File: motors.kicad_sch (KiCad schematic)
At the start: 32 parts, among them Q1 NMOS, Q2 NMOS, Q3 NMOS, Q4 NMOS

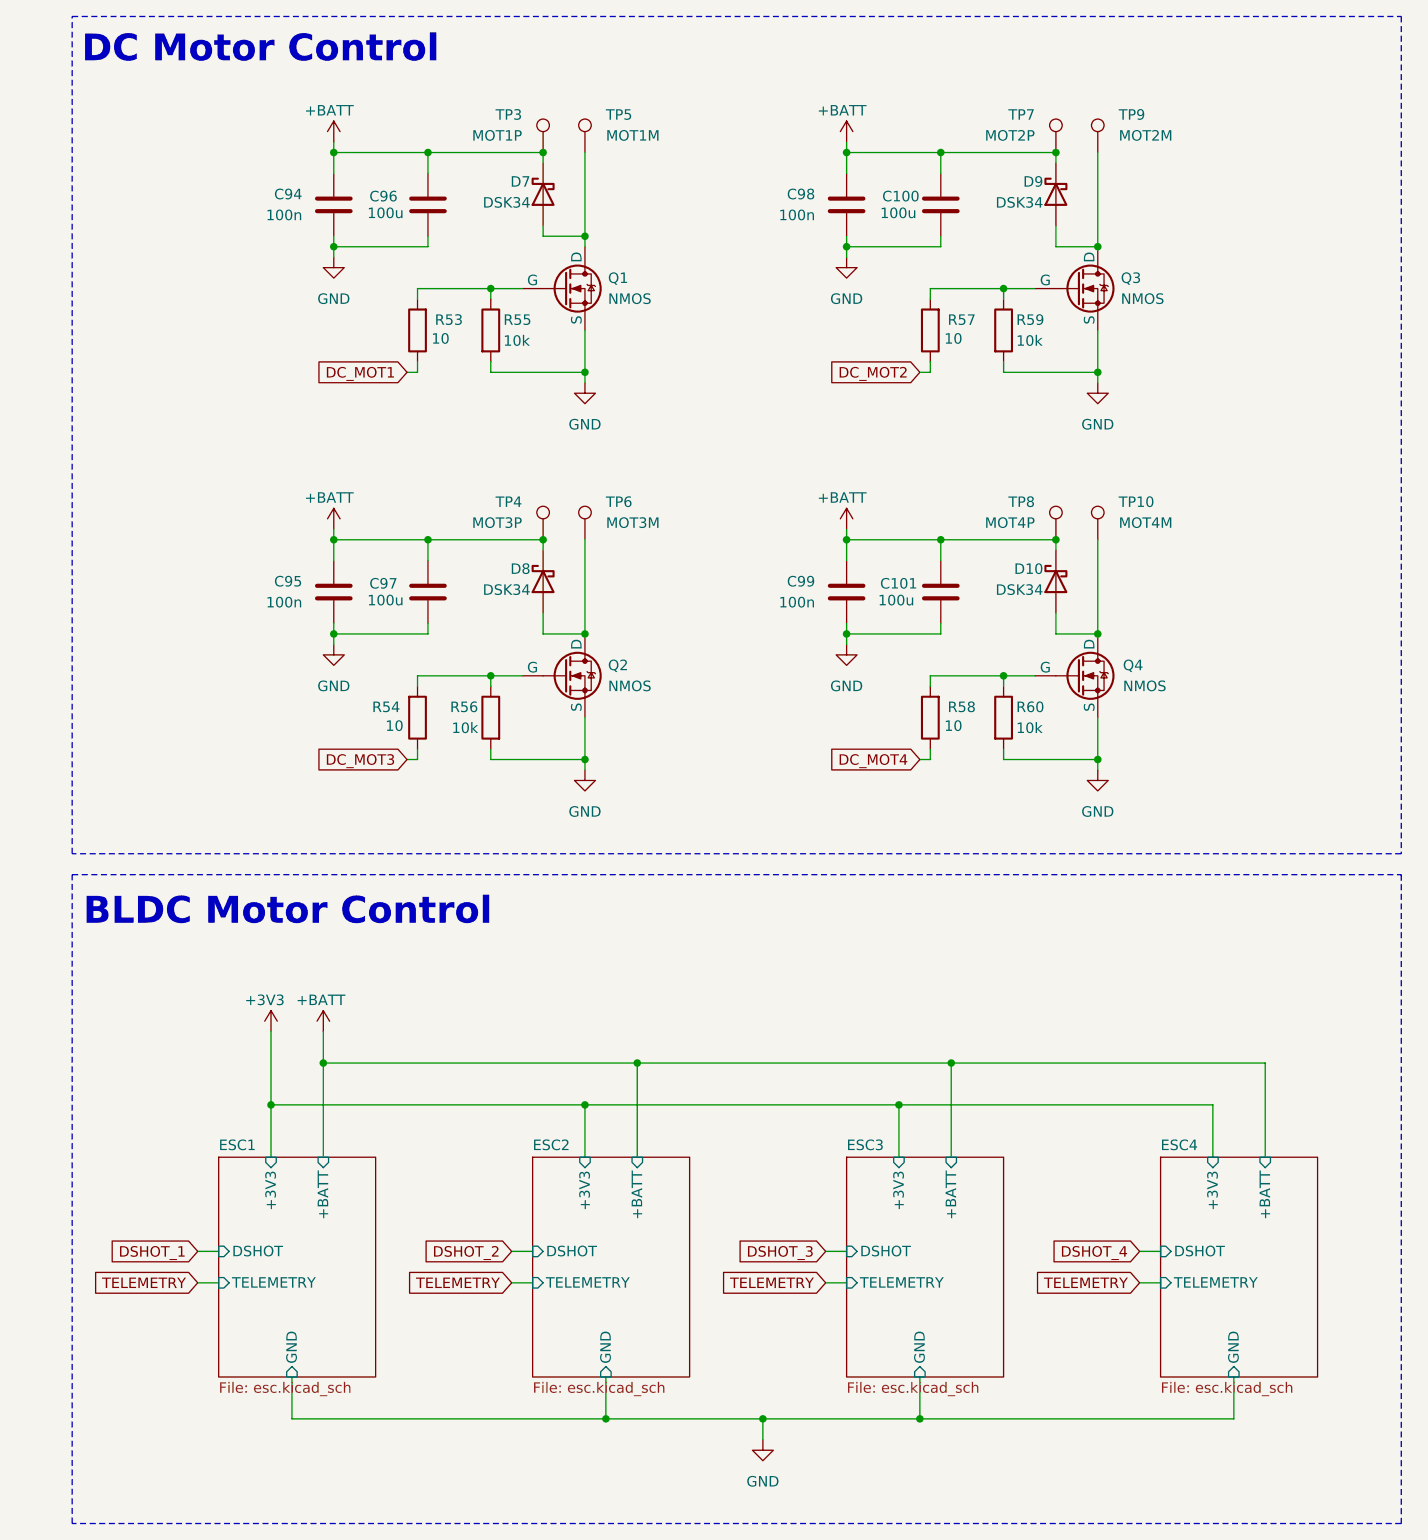
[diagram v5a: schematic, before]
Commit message: Remove brushed motor control and WS2812B LEDs
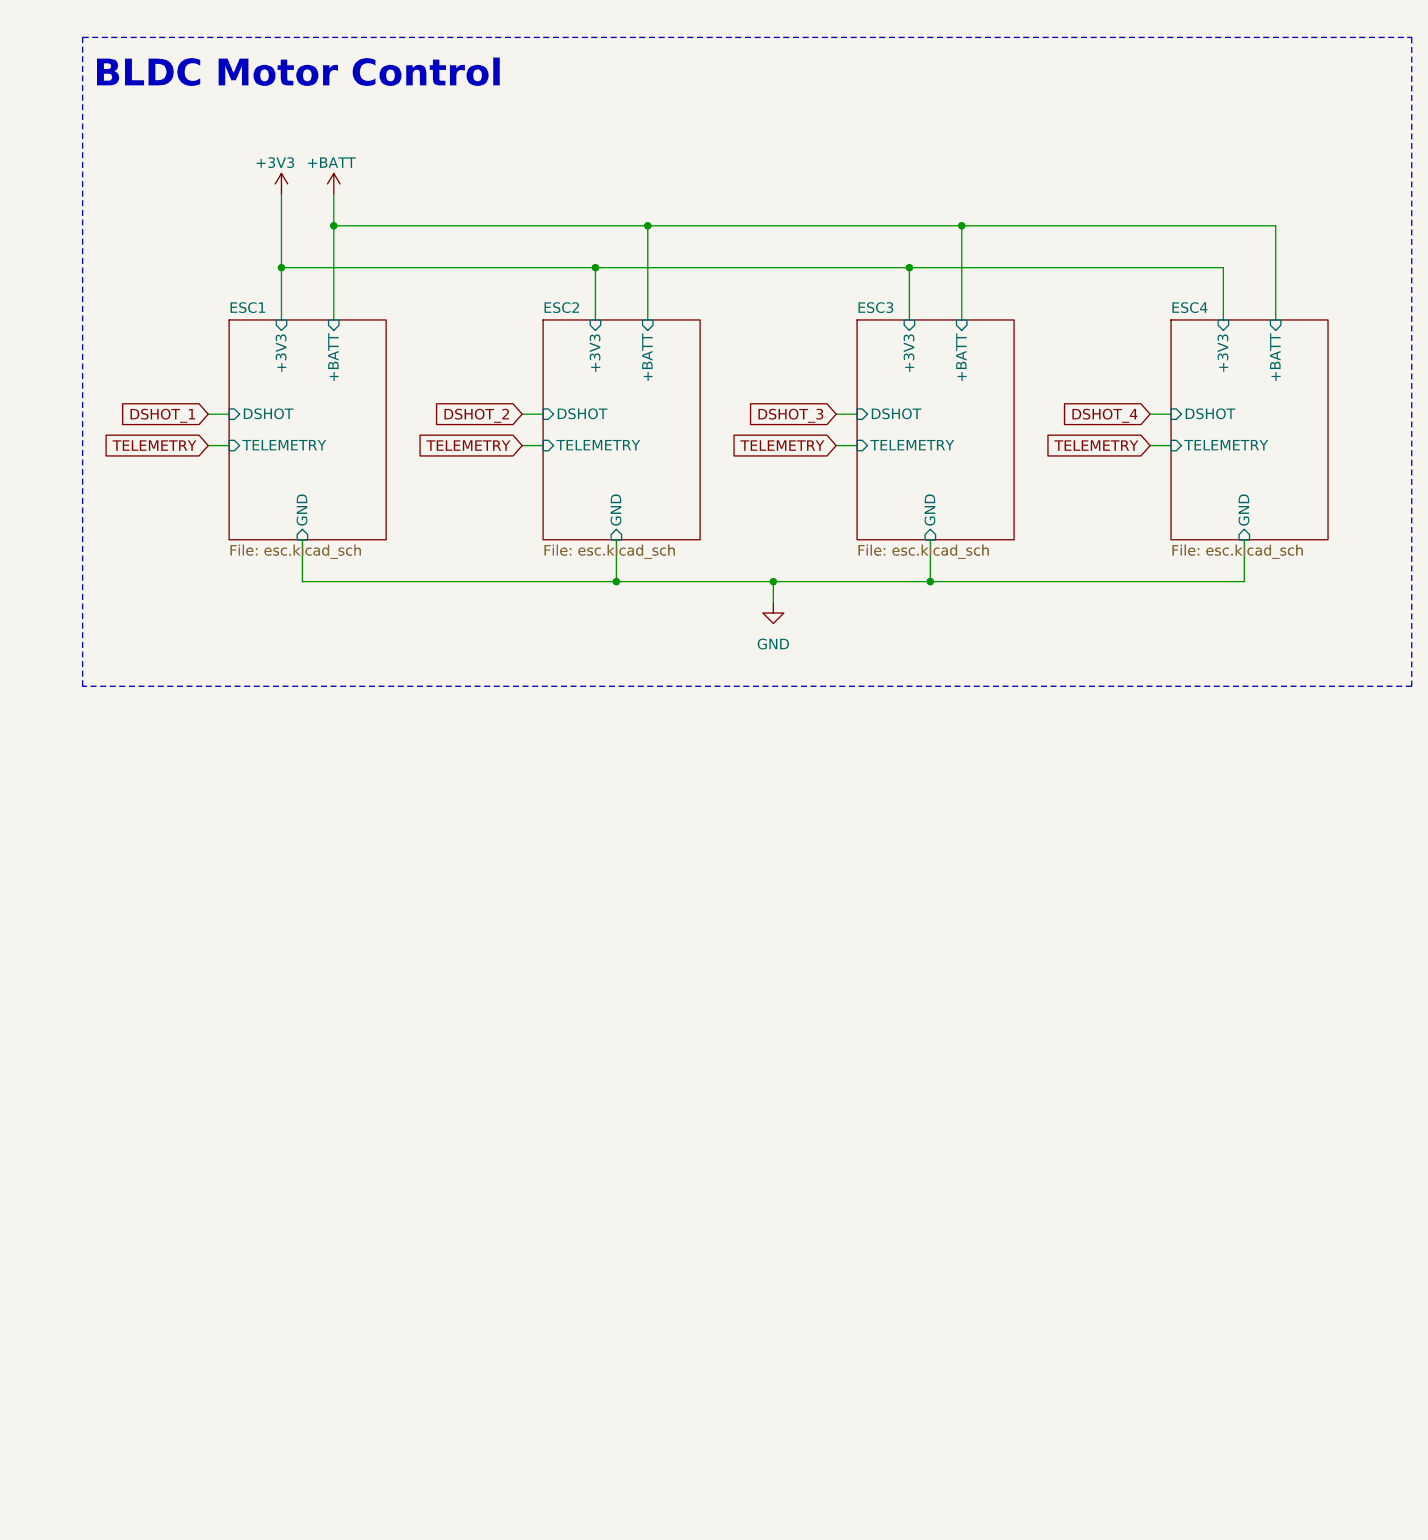
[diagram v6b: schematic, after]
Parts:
- removed C100, C101, C96, C97: 100u, Capacitor_SMD:C_1206_3216Metric, symbol Device:C
- removed C94, C95, C98, C99: 100n, Capacitor_SMD:C_0402_1005Metric, symbol Device:C
- removed D10, D7, D8, D9: DSK34, Diode_SMD:D_SOD-123F, symbol Device:D_Schottky
- removed Q1, Q2, Q3, Q4: NMOS, easyeda2kicad:SOT-23-IRLML6344, symbol Simulation_SPICE:NMOS
- removed R53, R54, R57, R58: 10, Resistor_SMD:R_0402_1005Metric, symbol Device:R
- removed R55, R56, R59, R60: 10k, Resistor_SMD:R_0402_1005Metric, symbol Device:R
- removed TP10: MOT4M, easyeda2kicad:MotorPad_1x3mm, symbol Connector:TestPoint
- removed TP3: MOT1P, easyeda2kicad:MotorPad_1x3mm, symbol Connector:TestPoint
- removed TP4: MOT3P, easyeda2kicad:MotorPad_1x3mm, symbol Connector:TestPoint
- removed TP5: MOT1M, easyeda2kicad:MotorPad_1x3mm, symbol Connector:TestPoint
- removed TP6: MOT3M, easyeda2kicad:MotorPad_1x3mm, symbol Connector:TestPoint
- removed TP7: MOT2P, easyeda2kicad:MotorPad_1x3mm, symbol Connector:TestPoint
- removed TP8: MOT4P, easyeda2kicad:MotorPad_1x3mm, symbol Connector:TestPoint
- removed TP9: MOT2M, easyeda2kicad:MotorPad_1x3mm, symbol Connector:TestPoint
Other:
- note removed: "DC Motor Control"

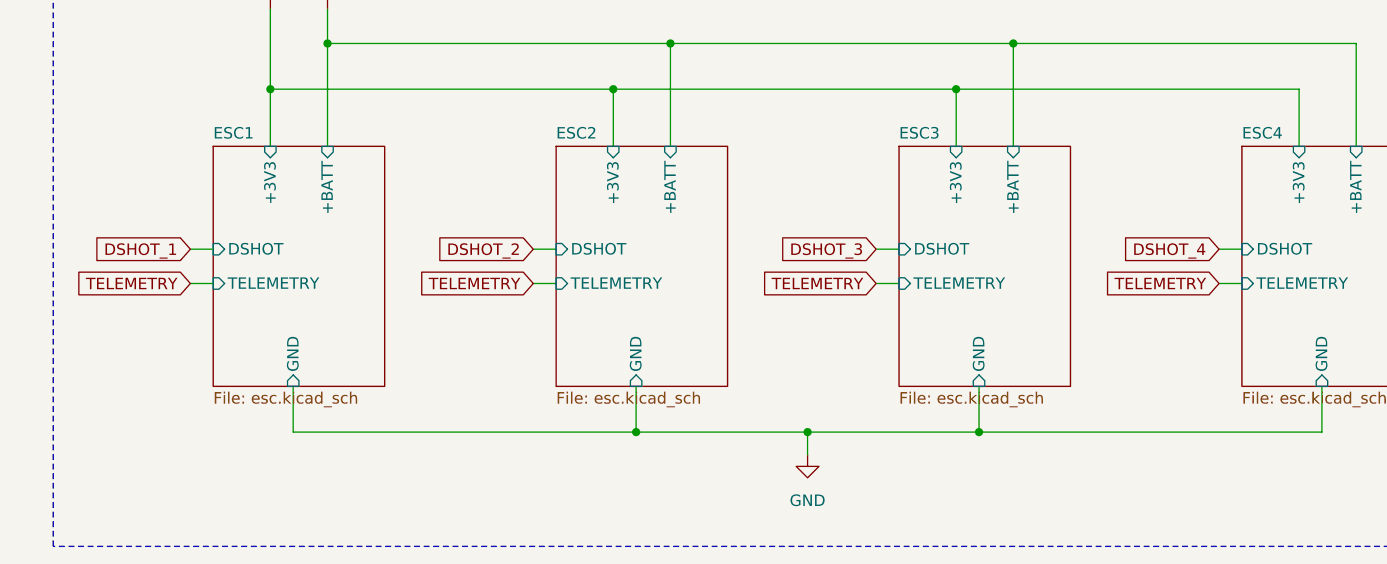
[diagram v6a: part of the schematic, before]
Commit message: Remove external SPI connections and switch voltage measurement from VBUS to +BAT
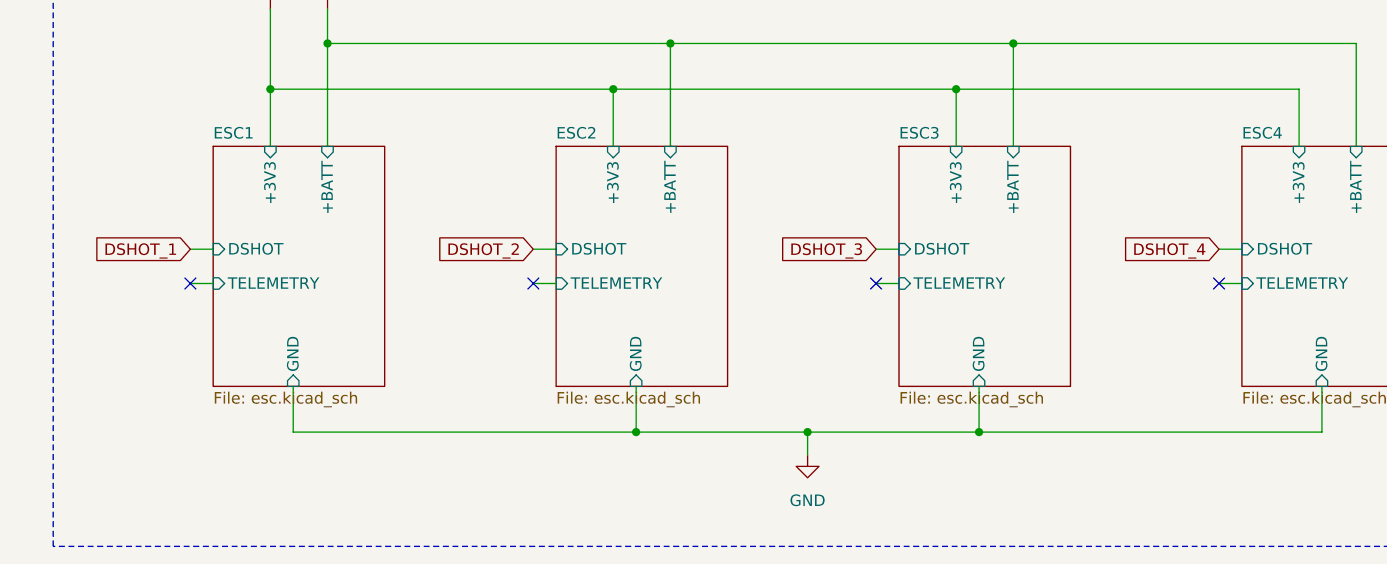
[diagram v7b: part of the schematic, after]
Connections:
- no-connect marks 0 -> 4
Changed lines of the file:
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@@
 		(color 0 0 0 0)
+	)
+	(no_connect
+		(at 144.78 66.04)
+	)
+	(no_connect
+		(at 68.58 66.04)
+	)
+	(no_connect
+		(at 106.68 66.04)
+	)
+	(no_connect
+		(at 30.48 66.04)
 	)
 	(wire
@@
 		)
 	)
-	(global_label "TELEMETRY"
-		(shape input)
-		(at 68.58 66.04 180)
-		(fields_autoplaced yes)
-		(effects
-			(font
-				(size 1.27 1.27)
-			)
-			(justify right)
-		)
-		(property "Intersheetrefs" "${INTERSHEET_REFS}"
-			(at 55.3745 66.04 0)
-			(hide yes)
-			(show_name no)
-			(do_not_autoplace no)
-			(effects
-				(font
-					(size 1.27 1.27)
-				)
-				(justify right)
-			)
-		)
-	)
 	(global_label "DSHOT_3"
 		(shape input)
@@
 		)
 	)
-	(global_label "TELEMETRY"
-		(shape input)
-		(at 144.78 66.04 180)
-		(fields_autoplaced yes)
-		(effects
-			(font
-				(size 1.27 1.27)
-			)
-			(justify right)
-		)
-		(property "Intersheetrefs" "${INTERSHEET_REFS}"
-			(at 131.5745 66.04 0)
-			(hide yes)
-			(show_name no)
-			(do_not_autoplace no)
-			(effects
-				(font
-					(size 1.27 1.27)
-				)
-				(justify right)
-			)
-		)
-	)
 	(global_label "DSHOT_4"
 		(shape input)
@@
 			(hide yes)
 			(show_name no)
-			(do_not_autoplace no)
-			(effects
-				(font
-					(size 1.27 1.27)
-				)
-				(justify right)
-			)
-		)
-	)
-	(global_label "TELEMETRY"
-		(shape input)
-		(at 106.68 66.04 180)
-		(fields_autoplaced yes)
-		(effects
-			(font
-				(size 1.27 1.27)
-			)
-			(justify right)
-		)
-		(property "Intersheetrefs" "${INTERSHEET_REFS}"
-			(at 93.4745 66.04 0)
-			(hide yes)
-			(show_name no)
-			(do_not_autoplace no)
-			(effects
-				(font
-					(size 1.27 1.27)
-				)
-				(justify right)
-			)
-		)
-	)
-	(global_label "TELEMETRY"
-		(shape input)
-		(at 30.48 66.04 180)
-		(fields_autoplaced yes)
-		(effects
-			(font
-				(size 1.27 1.27)
-			)
-			(justify right)
-		)
-		(property "Intersheetrefs" "${INTERSHEET_REFS}"
-			(at 17.2745 66.04 0)
-			(hide yes)
-			(show_name no)

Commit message: Clean up schematics a bit
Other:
- note added: "Brushless Motor Electronic Speed Control"
- note removed: "BLDC Motor Control"
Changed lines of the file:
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@@
 		)
 	)
-	(text "BLDC Motor Control"
+	(text "Brushless Motor Electronic Speed Control"
 		(exclude_from_sim no)
-		(at 41.402 21.082 0)
+		(at 70.612 21.59 0)
 		(effects
 			(font
